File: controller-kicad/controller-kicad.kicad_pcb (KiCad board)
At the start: 2 copper layers, 117 parts, among them J1 RJ45_Amphenol_RJMG1BD3B8K1ANR, J10 Conn_01x03_Female, J11 Conn_01x02_Female, J12 Conn_01x01, J13 Conn_01x03_Male, J14 Conn_01x05_Female, J2 Conn_01x02_Female, J3 Conn_01x02_Female, J4 Conn_01x02_Female, J5 Conn_01x02_Female, J6 Conn_01x03_Female, J7 Conn_01x03_Female, J8 Conn_01x03_Female, J9 Conn_01x03_Female, U1 STM32F407ZETx, U10 IPD60R600, U11 TL431DBZ, U12 AD8495, U13 TLP250, U14 NCP1117-5.0_TO252, U15 NCP1117-3.3_TO252, U2 MCP1416, U3 MCP1416, U4 IPD60R600, U5 IPD60R600, U6 LAN8742, U7 MCP1416, U8 MCP1416, U9 IPD60R600, Y1 25 MHz, Y2 25 MHz

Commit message: More progress on routing
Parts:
- C18, C24, C26, C28: moved to B.Cu
- moved J12 79.9 mm to (188.0, 73.9)
- moved R5 79.7 mm to (128.9, 87.6), turned to 180 degrees
- moved R4 73.3 mm to (128.9, 85.9), turned to 180 degrees
- moved R3 69.2 mm to (128.9, 83.8), turned to 180 degrees
- moved R15 67.9 mm to (146.8, 84.1)
- moved C24 67.4 mm to (145.0, 90.4), turned to -90 degrees
- moved C22 64.2 mm to (140.5, 80.0), turned to -90 degrees
- moved C20 63.1 mm to (155.2, 79.8), turned to 90 degrees
- moved C18 62.6 mm to (140.5, 80.0), turned to -90 degrees
- moved R9 62.2 mm to (150.1, 80.3), turned to 90 degrees
- moved R14 60.3 mm to (137.7, 92.7), turned to 180 degrees
- moved C28 58.7 mm to (137.7, 83.1), turned to 90 degrees
- moved R6 58.1 mm to (154.2, 83.3), turned to 180 degrees
- moved R18 57.0 mm to (137.7, 94.2), turned to 180 degrees
- moved C26 56.5 mm to (144.8, 81.3), turned to 90 degrees
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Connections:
- R11 pad 2: Net-(R11-Pad2) -> Net-(U6-Pad7)
- R12 pad 1: ETH_RXD0 -> Net-(U6-Pad8)
- R12 pad 2: Net-(R12-Pad2) -> ETH_RXD0
- R3 pad 1: ETH_RXD1 -> Net-(U6-Pad7)
- R4 pad 1: ETH_RXD0 -> Net-(U6-Pad8)
- U6 pad 7: Net-(R11-Pad2) -> Net-(U6-Pad7)
- U6 pad 8: Net-(R12-Pad2) -> Net-(U6-Pad8)
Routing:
- net ETH_LED1: track 0.00 -> 36.9 mm, vias 0 -> 1
- net Net-(C34-Pad1): track 0.00 -> 36.5 mm
- net Net-(C33-Pad1): track 0.00 -> 35.5 mm
- net Net-(C32-Pad1): track 0.00 -> 32.4 mm
- net Net-(C31-Pad1): track 0.00 -> 32.3 mm
- net ETH_LED2: track 0.00 -> 31.8 mm, vias 0 -> 1
- net Net-(C21-Pad2): track 0.00 -> 29.0 mm
- net Net-(C20-Pad2): track 0.00 -> 28.2 mm
- net ETH_CRS_DV: track 0.00 -> 23.1 mm, vias 0 -> 2
- net ETH_REF_CLK: track 0.00 -> 19.9 mm, vias 0 -> 2
- net Net-(R10-Pad1): track 0.00 -> 17.8 mm
- net ETH_RXD1: track 25.9 -> 9.40 mm
- net Net-(R6-Pad2): track 0.00 -> 13.5 mm
- net Net-(U6-Pad7): track 0.00 -> 13.4 mm
- net VBAT: track 0.00 -> 13.0 mm, vias 0 -> 3
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
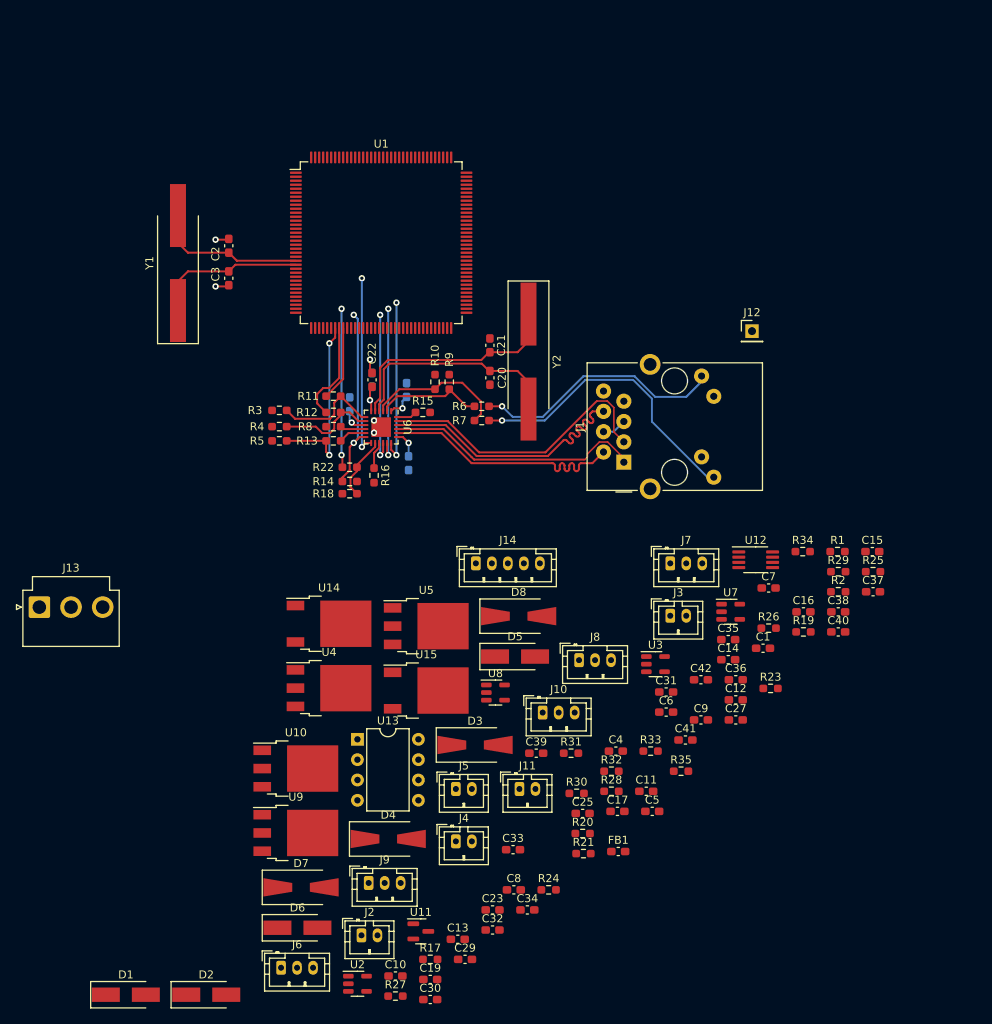
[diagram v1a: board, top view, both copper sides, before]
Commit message: Got all components onto PCB
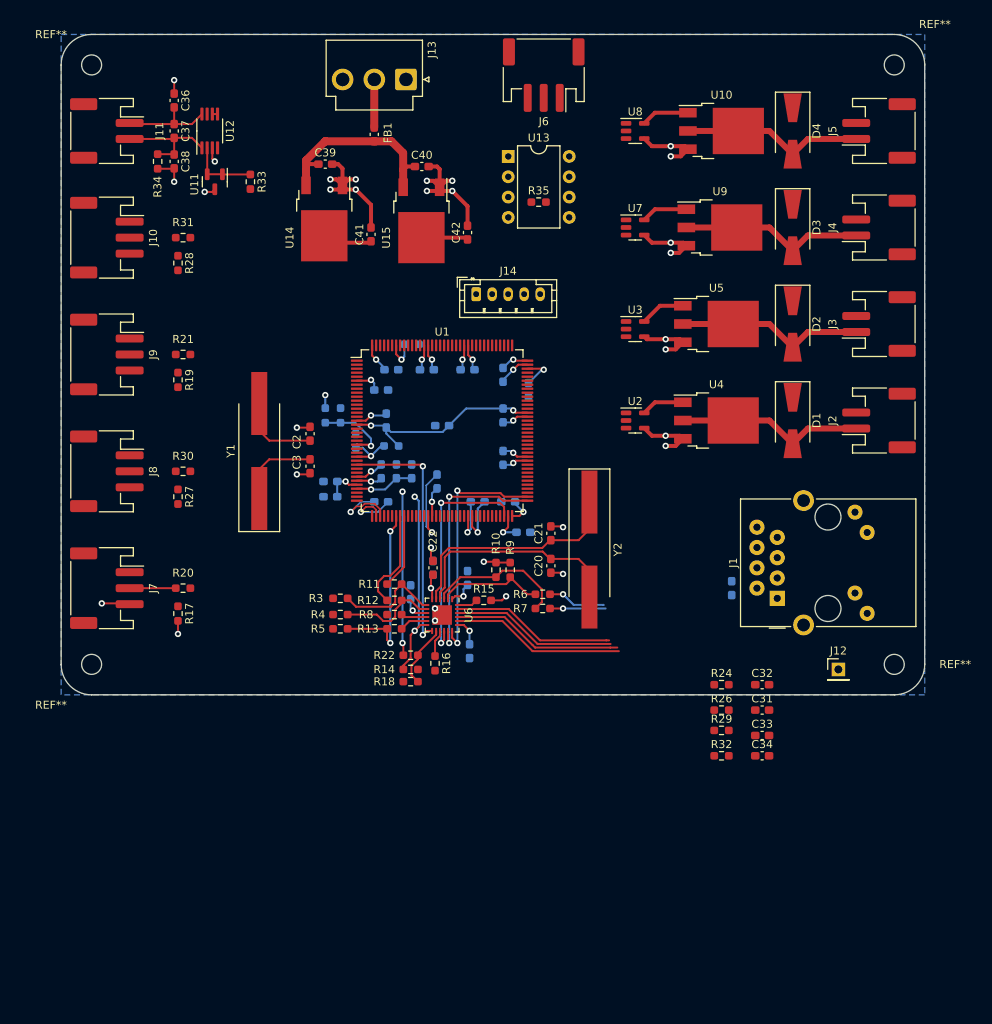
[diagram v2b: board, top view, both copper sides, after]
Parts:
- removed D5, D6: D_Zener_Small, Diode_SMD:D_SMA_Handsoldering
- removed D7, D8: D_Small, Diode_SMD:D_SMA-SMB_Universal_Handsoldering
- added REF**: MountingHole_2.5mm, MountingHole:MountingHole_2.5mm, F.Cu at (105.4, 115.6)
- added REF**: MountingHole_2.5mm, MountingHole:MountingHole_2.5mm, F.Cu at (205.7, 40.6)
- added REF**: MountingHole_2.5mm, MountingHole:MountingHole_2.5mm, F.Cu at (205.7, 115.6)
- added REF**: MountingHole_2.5mm, MountingHole:MountingHole_2.5mm, F.Cu at (105.4, 40.6)
- C1, C10, C11, C12, C13, C14, C15, C16, C17, C19, C23, C25, C27, C29, C30, C35, C4, C5, C6, C7, C8, C9, R1, R2, R23, R25: moved to B.Cu
- D1, D2: value D_Zener_Small -> D_Small; footprint Diode_SMD:D_SMA_Handsoldering -> Diode_SMD:D_SMA-SMB_Universal_Handsoldering
- J10, J6, J7, J8, J9: footprint Connector_JST:JST_PH_B3B-PH-K_1x03_P2.00mm_Vertical -> Connector_JST:JST_PH_S3B-PH-SM4-TB_1x03-1MP_P2.00mm_Horizontal
- J11, J2, J3, J4, J5: footprint Connector_JST:JST_PH_B2B-PH-K_1x02_P2.00mm_Vertical -> Connector_JST:JST_PH_S2B-PH-SM4-TB_1x02-1MP_P2.00mm_Horizontal
- moved J6 116.3 mm to (161.9, 41.9), turned to 180 degrees
- moved D2 111.4 mm to (193.0, 73.0), turned to -90 degrees
- moved D1 110.0 mm to (193.0, 85.1), turned to -90 degrees
- moved C37 104.6 mm to (115.7, 48.9), turned to -90 degrees
- moved D4 101.9 mm to (193.0, 48.9), turned to -90 degrees
- moved C36 100.9 mm to (115.7, 45.1), turned to -90 degrees
- moved C38 100.3 mm to (115.7, 52.7), turned to -90 degrees
- moved J5 97.8 mm to (203.8, 48.9), turned to 90 degrees
- moved U11 97.2 mm to (120.8, 55.2), turned to -90 degrees
- moved J11 97.1 mm to (107.3, 48.9), turned to -90 degrees
- moved U10 95.8 mm to (184.2, 48.9)
- moved FB1 94.7 mm to (140.7, 49.3), turned to 90 degrees
- moved R34 94.2 mm to (113.7, 52.7), turned to -90 degrees
- moved J4 93.2 mm to (203.8, 61.0), turned to 90 degrees
- moved U9 92.4 mm to (184.0, 61.0)
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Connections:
- D1 pad 1: SV1 -> Vdrive
- D1 pad 2: Net-(D1-Pad2) -> SV1
- D2 pad 1: SV2 -> Vdrive
- D2 pad 2: Net-(D2-Pad2) -> SV2
- D3 pad 2: Net-(D1-Pad2) -> SV3
- D4 pad 2: Net-(D2-Pad2) -> SV4
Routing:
- net GND: track 5.19 -> 140.7 mm, vias 5 -> 41
- net VBAT: track 13.0 -> 101.7 mm, vias 3 -> 19
- net ETH_LED1: track 36.9 -> 6.96 mm
- net +12V: track 0.00 -> 24.5 mm
- net ETH_LED2: track 31.8 -> 7.26 mm
- net SV2: track 0.00 -> 23.7 mm
- net SV1: track 0.00 -> 23.7 mm
- net SV3: track 0.00 -> 23.2 mm
- net SV4: track 0.00 -> 23.0 mm
- net Net-(C34-Pad1): track 36.5 -> 20.5 mm
- net Net-(C33-Pad1): track 35.5 -> 20.7 mm
- net TS1-: track 0.00 -> 13.0 mm
- net Net-(C32-Pad1): track 32.4 -> 21.5 mm
- net TS1+: track 0.00 -> 10.9 mm
- net Net-(C31-Pad1): track 32.3 -> 21.7 mm
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- added copper zone on B.Cu, net GND
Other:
- board outline added: 108 x 82.5 mm

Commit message: Routing mostly finished
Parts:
- C31, C32, C33, C34, R35: moved to B.Cu
- moved J10 43.8 mm to (107.3, 106.0)
- moved R31 43.8 mm to (116.8, 106.0)
- moved R28 43.8 mm to (116.2, 109.2)
- moved J7 43.2 mm to (107.0, 62.9)
- moved R20 43.2 mm to (116.5, 62.9)
- moved R17 43.2 mm to (115.9, 66.0)
- moved D4 37.2 mm to (193.0, 86.1)
- moved J5 37.2 mm to (203.8, 86.1)
- moved U10 37.2 mm to (184.1, 86.1)
- moved U8 37.2 mm to (173.3, 86.1)
- moved D1 36.4 mm to (193.0, 48.7)
- moved J2 36.4 mm to (203.8, 48.7)
- moved U2 36.4 mm to (173.4, 48.7)
- moved U4 36.4 mm to (183.5, 48.7)
- moved C33 23.9 mm to (184.8, 101.0), turned to 180 degrees
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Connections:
- net Net-(C31-Pad1) renamed /TX-
- net Net-(C32-Pad1) renamed /TX+
- net Net-(C33-Pad1) renamed /RX-
- net Net-(C34-Pad1) renamed /RX+
- J6 pad 2: SPARK_GND -> SPARK
- J6 pad 3: SPARK -> SPARK_GND
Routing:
- net VBAT: track 101.7 -> 183.7 mm, vias 19 -> 54
- net +12V: track 24.5 -> 104.5 mm, vias 0 -> 6
- net ADC1_IN3: track 0.00 -> 65.6 mm
- net ADC1_IN4: track 0.00 -> 53.4 mm
- net SPARK_CTRL: track 0.00 -> 49.9 mm, vias 0 -> 1
- net ADC3_IN7: track 0.65 -> 49.5 mm
- net ETH_LED1: track 6.96 -> 50.8 mm
- net ADC2_IN5: track 0.00 -> 40.2 mm
- net ETH_LED2: track 7.26 -> 46.8 mm
- net SV1_CTRL: track 0.00 -> 36.9 mm
- net /RX+: track 20.5 -> 57.1 mm
- net /RX-: track 20.7 -> 57.0 mm
- net ADC2_IN6: track 0.00 -> 33.0 mm
- net /TX+: track 21.5 -> 53.7 mm
- net /TX-: track 21.7 -> 53.5 mm
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- added copper zone on F.Cu, net +5V
- added copper zone on F.Cu, net VBAT
- added copper zone on F.Cu, net Vdrive
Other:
- board text added: "SV1"
- board text added: "SV2"
- board text added: "SV3"
- board text added: "SV4"

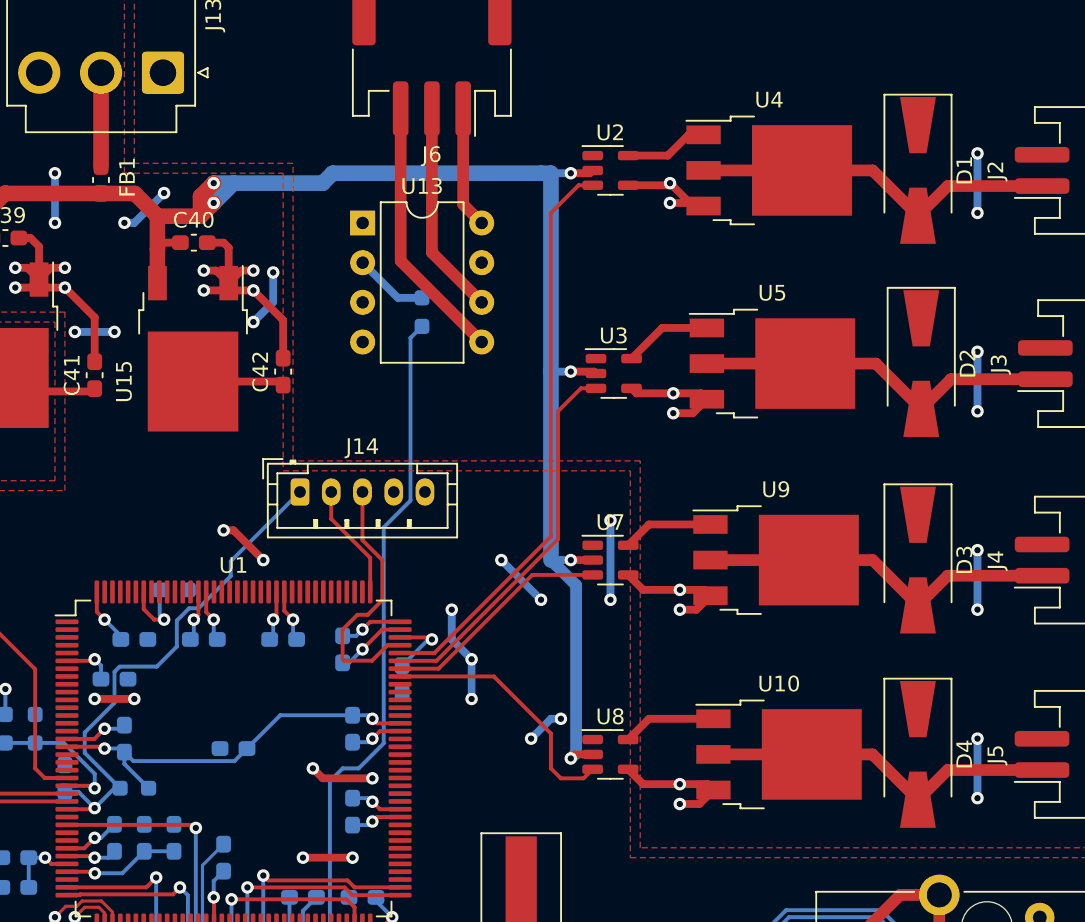
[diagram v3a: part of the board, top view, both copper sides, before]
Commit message: Added reset button to PCB
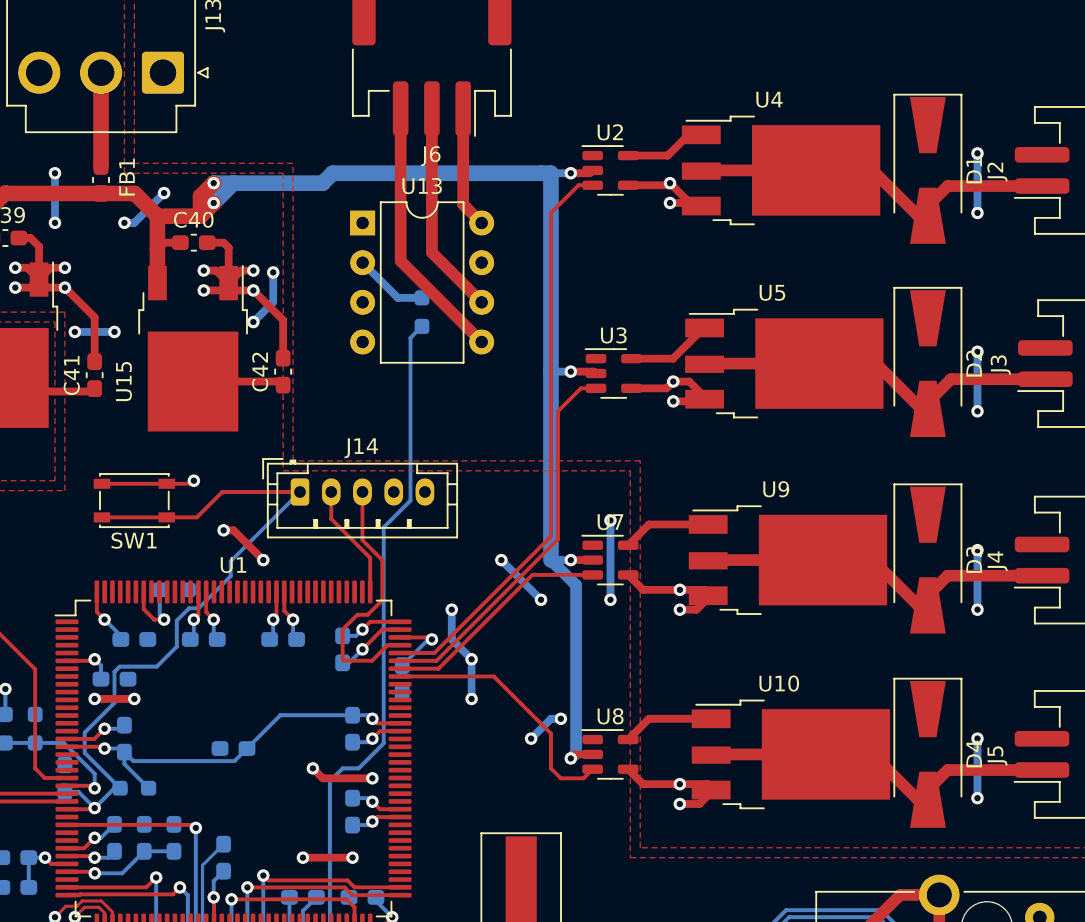
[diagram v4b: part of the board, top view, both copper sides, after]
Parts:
- added SW1: SW_RST, Button_Switch_SMD:SW_SPST_PTS810, F.Cu at (142.9, 69.8)
- U10, U4, U5, U9: footprint Package_TO_SOT_SMD:TO-252-3_TabPin2 -> custom_footprints:TO-252-3_TabPin2-HandSolder
- moved D4 0.64 mm to (193.7, 86.1)
- moved D1 0.64 mm to (193.7, 48.7)
- moved D3 0.64 mm to (193.7, 73.7)
- moved D2 0.43 mm to (193.7, 61.1)
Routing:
- net RST: track 33.6 -> 47.0 mm
- net GND: track 171.3 -> 177.3 mm, vias 57 -> 58

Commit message: Hopefully finished board
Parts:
- added D5: LED_Small, LED_SMD:LED_0603_1608Metric_Pad1.05x0.95mm_HandSolder, F.Cu at (135.9, 73.7)
- added J15: Conn_01x03_Female, Connector_JST:JST_PH_S3B-PH-SM4-TB_1x03-1MP_P2.00mm_Horizontal, F.Cu at (107.0, 49.5)
- added R36: 220, Resistor_SMD:R_0603_1608Metric_Pad0.98x0.95mm_HandSolder, B.Cu at (134.6, 73.7)
- C2, C3: value 27pF -> 23pF
- R23, R25: moved to F.Cu
- moved R25 30.5 mm to (116.8, 59.7), turned to 180 degrees
- moved R23 29.7 mm to (116.8, 62.2), turned to -90 degrees
- moved J11 16.9 mm to (122.8, 42.0), turned to 180 degrees
- moved C36 12.1 mm to (126.6, 50.5), turned to 180 degrees
- moved C37 7.20 mm to (122.8, 50.5), turned to 180 degrees
- moved R34 6.82 mm to (119.0, 48.4), turned to 180 degrees
- moved U12 6.04 mm to (122.9, 54.3), turned to 0 degrees
- moved R33 4.40 mm to (121.3, 57.1), turned to 0 degrees
- moved U11 4.28 mm to (116.5, 54.9), turned to 180 degrees
- moved C38 3.93 mm to (119.0, 50.5), turned to 180 degrees
- moved R20 3.81 mm to (116.5, 66.7)
- moved R17 3.81 mm to (115.9, 69.8)
- moved D1 0.63 mm to (194.3, 48.7)
- moved D2 0.63 mm to (194.3, 61.1)
- moved D3 0.63 mm to (194.3, 73.7)
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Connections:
- R25 pad 2: VBAT -> PS5
- U1 pad 4: unconnected-(U1-Pad4) -> Net-(D5-Pad2)
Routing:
- net ADC3_IN8: track 9.29 -> 43.6 mm, vias 1 -> 0
- net PS5: track 0.00 -> 15.1 mm
- net VBAT: track 183.7 -> 198.6 mm, vias 54 -> 61
- net ADC3_IN7: track 49.5 -> 39.4 mm
- net Net-(D5-Pad2): track 0.00 -> 7.53 mm
- net +5V: track 31.0 -> 37.0 mm, vias 16 -> 18
- net GND: track 177.3 -> 183.3 mm, vias 58 -> 60
- net Vdrive: track 15.2 -> 20.3 mm, vias 8 -> 12
- net Net-(D5-Pad1): track 0.00 -> 4.56 mm, vias 0 -> 1
- net ADC1_IN3: track 65.6 -> 63.3 mm
- net PS1: track 5.76 -> 7.91 mm
- net /TX-: track 53.5 -> 54.3 mm
- net TS1-: track 13.0 -> 12.3 mm
- net TS1+: track 11.7 -> 11.1 mm
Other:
- board text added: "PS1"
- board text added: "PS2"
- board text added: "PS3"
- board text added: "PS4"
- board text added: "PS5"
- board text added: "SPARK"
- board text added: "TS1"
